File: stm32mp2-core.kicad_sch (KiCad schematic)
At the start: 0 parts

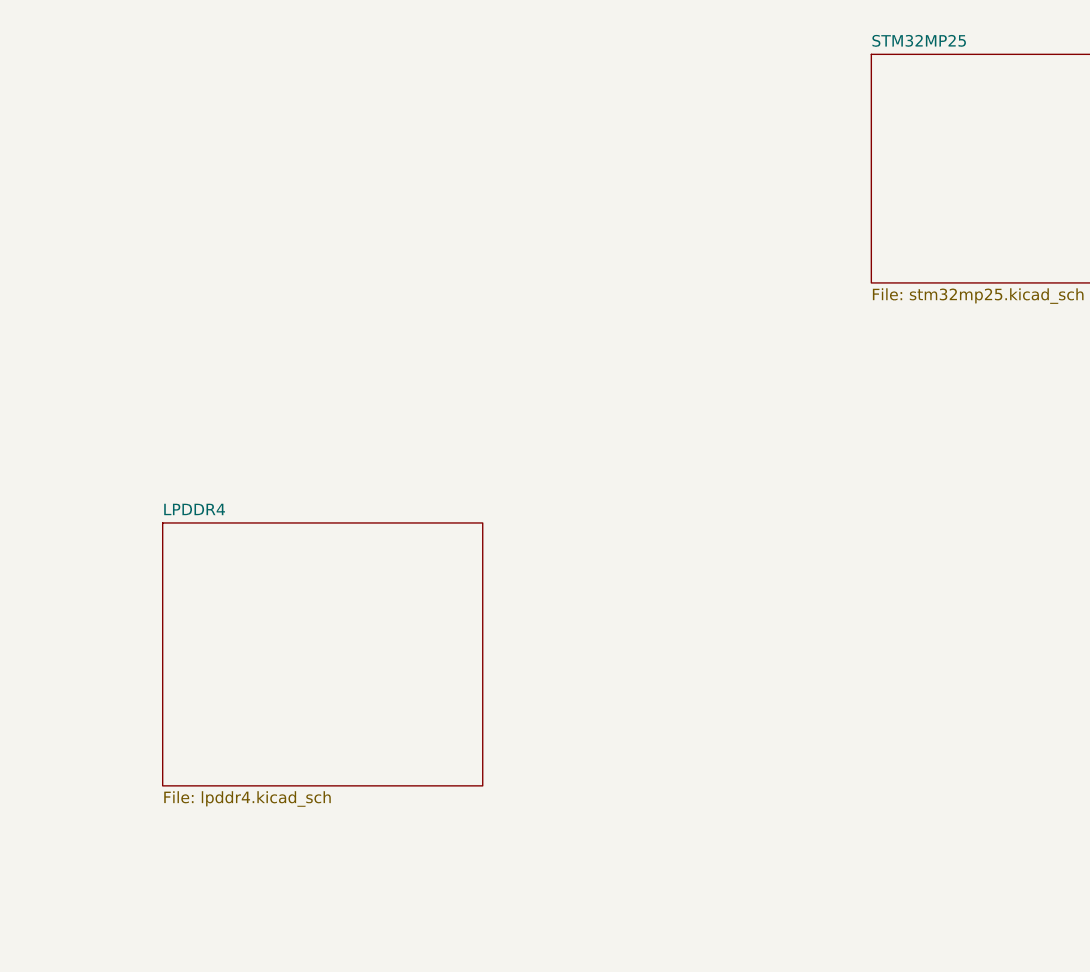
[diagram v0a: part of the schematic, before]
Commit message: connected lpddr4 to mp
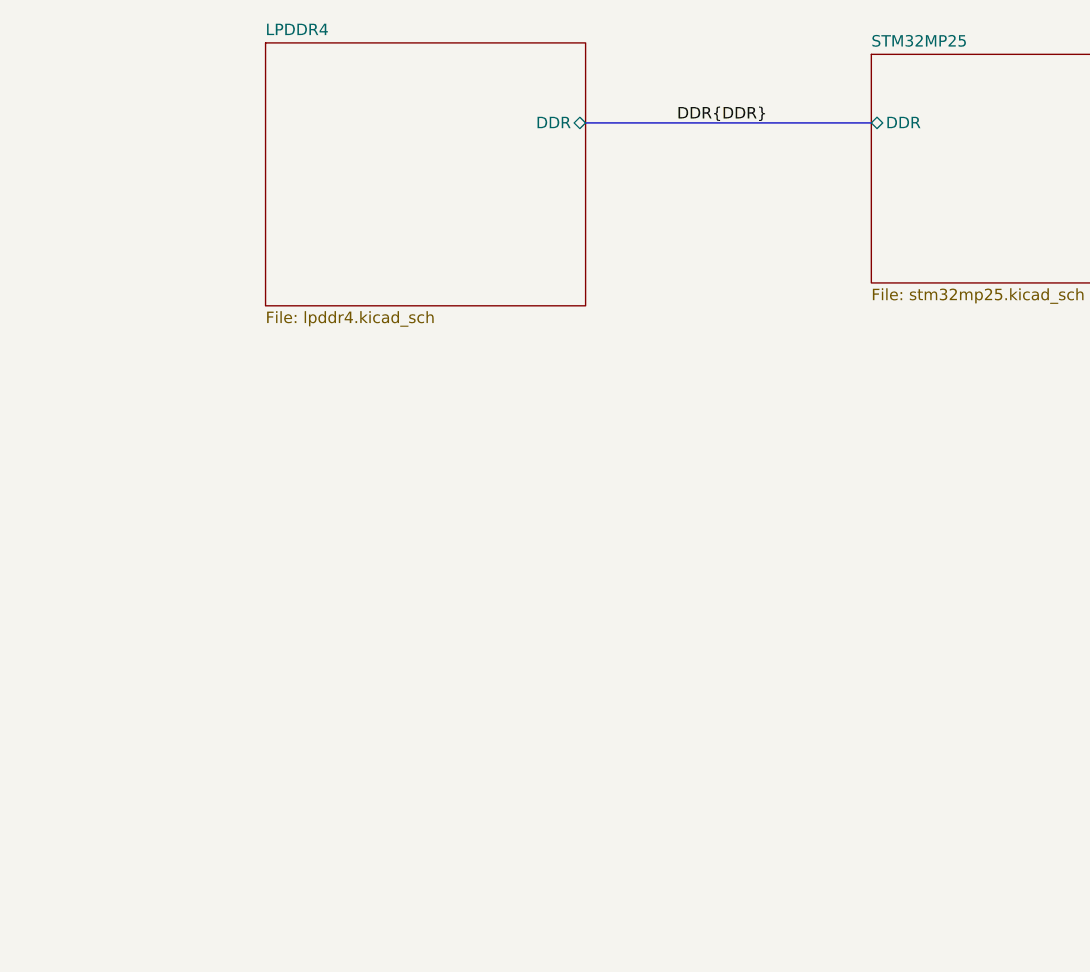
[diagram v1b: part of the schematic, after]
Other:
- sheet LPDDR4 ports: added DDR; removed none
- sheet STM32MP25 ports: added DDR; removed none
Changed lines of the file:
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@@
+		)
+	)
+	(bus
+		(pts
+			(xy 90.17 53.34) (xy 121.92 53.34)
+		)
+		(stroke
+			(width 0)
+			(type default)
+		)
+	)
+	(label "DDR{DDR}"
+		(at 100.33 53.34 0)
+		(effects
+			(font
+				(size 1.27 1.27)
+			)
+			(justify left bottom)
 		)
 	)
 	(sheet
-		(at 43.18 97.79)
+		(at 54.61 44.45)
 		(size 35.56 29.21)
 		(exclude_from_sim no)
@@
 		)
 		(property "Sheetname" "LPDDR4"
-			(at 43.18 97.0784 0)
+			(at 54.61 43.7384 0)
 			(effects
 				(font
@@
 		)
 		(property "Sheetfile" "lpddr4.kicad_sch"
-			(at 43.18 127.5846 0)
+			(at 54.61 74.2446 0)
 			(effects
 				(font
@@
 				)
 				(justify left top)
+			)
+		)
+		(pin "DDR" bidirectional
+			(at 90.17 53.34 0)
+			(effects
+				(font
+					(size 1.27 1.27)
+				)
+				(justify right)
 			)
 		)
@@
 			)
 		)
+		(pin "DDR" bidirectional
+			(at 121.92 53.34 180)
+			(effects
+				(font
+					(size 1.27 1.27)
+				)
+				(justify left)
+			)
+		)

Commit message: got started on the pmic
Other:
- added sheet PMIC (pmic.kicad_sch)
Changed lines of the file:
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@@
 	)
 	(sheet
-		(at 54.61 44.45)
-		(size 35.56 29.21)
+		(at 194.31 44.45)
+		(size 29.21 25.4)
+		(exclude_from_sim no)
+		(in_bom yes)
+		(on_board yes)
+		(dnp no)
+		(fields_autoplaced yes)
+		(stroke
+			(width 0.1524)
+			(type solid)
+		)
+		(fill
+			(color 0 0 0 0.0000)
+		)
+		(property "Sheetname" "PMIC"
+			(at 194.31 43.7384 0)
+			(effects
+				(font
+					(size 1.27 1.27)
+				)
+				(justify left bottom)
+			)
+		)
+		(property "Sheetfile" "pmic.kicad_sch"
+			(at 194.31 70.4346 0)
+			(effects
+				(font
+					(size 1.27 1.27)
+				)
+				(justify left top)
+			)
+		)
+		(instances
+			(project "stm32mp2-core"
+				(path "/5f8e630b-79db-437a-bc04-3ab5a18328d4"
+					(page "9")
+				)
+			)
+		)
+	)
+	(sheet
+		(at 60.96 45.72)
+		(size 29.21 26.67)
 		(exclude_from_sim no)
 		(in_bom yes)
@@
 		)
 		(property "Sheetname" "LPDDR4"
-			(at 54.61 43.7384 0)
+			(at 60.96 45.0084 0)
 			(effects
 				(font
@@
 		)
 		(property "Sheetfile" "lpddr4.kicad_sch"
-			(at 54.61 74.2446 0)
+			(at 60.96 72.9746 0)
 			(effects
 				(font

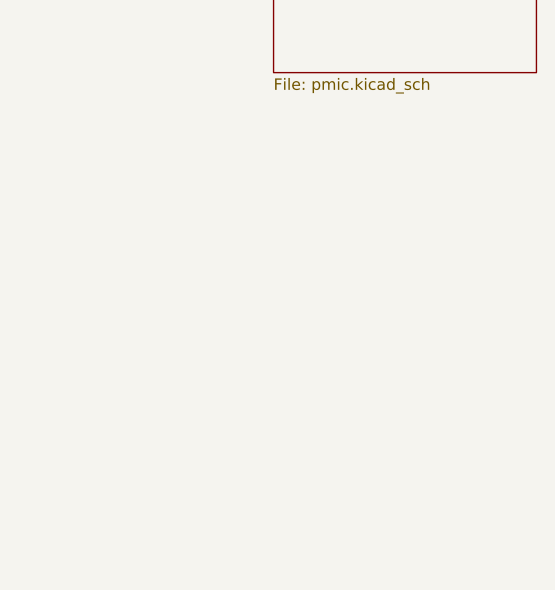
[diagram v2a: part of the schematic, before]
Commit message: added sd card holder for fun
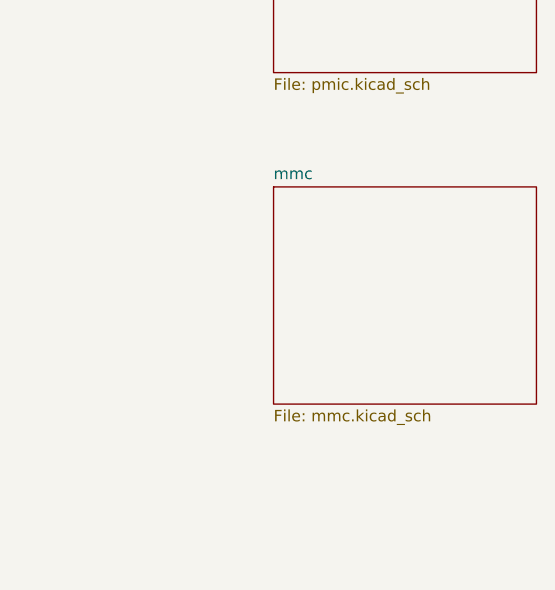
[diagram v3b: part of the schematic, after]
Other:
- added sheet mmc (mmc.kicad_sch)
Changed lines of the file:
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@@
+		)
+	)
+	(sheet
+		(at 194.31 82.55)
+		(size 29.21 24.13)
+		(exclude_from_sim no)
+		(in_bom yes)
+		(on_board yes)
+		(dnp no)
+		(fields_autoplaced yes)
+		(stroke
+			(width 0.1524)
+			(type solid)
+		)
+		(fill
+			(color 0 0 0 0.0000)
+		)
+		(property "Sheetname" "mmc"
+			(at 194.31 81.8384 0)
+			(effects
+				(font
+					(size 1.27 1.27)
+				)
+				(justify left bottom)
+			)
+		)
+		(property "Sheetfile" "mmc.kicad_sch"
+			(at 194.31 107.2646 0)
+			(effects
+				(font
+					(size 1.27 1.27)
+				)
+				(justify left top)
+			)
+		)
+		(instances
+			(project "stm32mp2-core"
+				(path "/5f8e630b-79db-437a-bc04-3ab5a18328d4"
+					(page "10")
+				)
+			)
 		)
 	)
